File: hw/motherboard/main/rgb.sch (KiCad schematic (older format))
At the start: 68 parts, among them Q1 BSS138

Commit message: WIP Start motherboard PCB layout.
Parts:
- renumbered D6 to D10, D10 to D11, D14 to D12, D18 to D13, D22 to D14, D26 to D15, D30 to D16, D3 to D17, D7 to D18, D11 to D19, D5 to D2, D15 to D20, D19 to D21, D23 to D22, D27 to D23, D31 to D24, D4 to D25, D8 to D26, D12 to D27, D16 to D28, D20 to D29, D9 to D3, D24 to D30, D28 to D31, D13 to D4, D17 to D5, D21 to D6, D25 to D7, D29 to D8, D2 to D9
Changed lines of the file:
@@
 $EndComp
 $Comp
-L LED:WS2812B D5
+L LED:WS2812B D2
 U 1 1 5E462888
 P 5400 1700
-F 0 "D5" H 5450 2000 50  0000 L CNN
+F 0 "D2" H 5450 2000 50  0000 L CNN
 F 1 "WS2812B" H 5450 1400 50  0000 L CNN
 F 2 "LED_SMD:LED_WS2812B_PLCC4_5.0x5.0mm_P3.2mm" H 5450 1400 50  0001 L TNN
@@
 $EndComp
 $Comp
-L LED:WS2812B D9
+L LED:WS2812B D3
 U 1 1 5E462931
 P 6000 1700
-F 0 "D9" H 6050 2000 50  0000 L CNN
+F 0 "D3" H 6050 2000 50  0000 L CNN
 F 1 "WS2812B" H 6050 1400 50  0000 L CNN
 F 2 "LED_SMD:LED_WS2812B_PLCC4_5.0x5.0mm_P3.2mm" H 6050 1400 50  0001 L TNN
@@
 $EndComp
 $Comp
-L LED:WS2812B D13
+L LED:WS2812B D4
 U 1 1 5E462AA8
 P 6600 1700
-F 0 "D13" H 6650 2000 50  0000 L CNN
+F 0 "D4" H 6650 2000 50  0000 L CNN
 F 1 "WS2812B" H 6650 1400 50  0000 L CNN
 F 2 "LED_SMD:LED_WS2812B_PLCC4_5.0x5.0mm_P3.2mm" H 6650 1400 50  0001 L TNN
@@
 $EndComp
 $Comp
-L LED:WS2812B D17
+L LED:WS2812B D5
 U 1 1 5E462B55
 P 7200 1700
-F 0 "D17" H 7250 2000 50  0000 L CNN
+F 0 "D5" H 7250 2000 50  0000 L CNN
 F 1 "WS2812B" H 7250 1400 50  0000 L CNN
 F 2 "LED_SMD:LED_WS2812B_PLCC4_5.0x5.0mm_P3.2mm" H 7250 1400 50  0001 L TNN
@@
 $EndComp
 $Comp
-L LED:WS2812B D21
-U 1 1 5E462CD2
-P 7800 1700
-F 0 "D21" H 7850 2000 50  0000 L CNN
-F 1 "WS2812B" H 7850 1400 50  0000 L CNN
-F 2 "LED_SMD:LED_WS2812B_PLCC4_5.0x5.0mm_P3.2mm" H 7850 1400 50  0001 L TNN
-F 3 "https://cdn-shop.adafruit.com/datasheets/WS2812B.pdf" H 7900 1325 50  0001 L TNN
-	1    7800 1700
-	1    0    0    -1
-$EndComp
-$Comp
 L power:+5V #PWR065
 U 1 1 5E462CD9
@@
 $EndComp
 $Comp
-L LED:WS2812B D25
+L LED:WS2812B D7
 U 1 1 5E462D8B
 P 8400 1700
-F 0 "D25" H 8450 2000 50  0000 L CNN
+F 0 "D7" H 8450 2000 50  0000 L CNN
 F 1 "WS2812B" H 8450 1400 50  0000 L CNN
 F 2 "LED_SMD:LED_WS2812B_PLCC4_5.0x5.0mm_P3.2mm" H 8450 1400 50  0001 L TNN
@@
 $EndComp
 $Comp
-L LED:WS2812B D29
+L LED:WS2812B D8
 U 1 1 5E462E3E
 P 9000 1700
-F 0 "D29" H 9050 2000 50  0000 L CNN
+F 0 "D8" H 9050 2000 50  0000 L CNN
 F 1 "WS2812B" H 9050 1400 50  0000 L CNN
 F 2 "LED_SMD:LED_WS2812B_PLCC4_5.0x5.0mm_P3.2mm" H 9050 1400 50  0001 L TNN
@@
 $EndComp
 $Comp
-L LED:WS2812B D2
+L LED:WS2812B D9
 U 1 1 5E463575
 P 4800 2800
-F 0 "D2" H 4850 3100 50  0000 L CNN
+F 0 "D9" H 4850 3100 50  0000 L CNN
 F 1 "WS2812B" H 4850 2500 50  0000 L CNN
 F 2 "LED_SMD:LED_WS2812B_PLCC4_5.0x5.0mm_P3.2mm" H 4850 2500 50  0001 L TNN
@@
 $EndComp
 $Comp
-L LED:WS2812B D6
+L LED:WS2812B D10
 U 1 1 5E463588
 P 5400 2800
-F 0 "D6" H 5450 3100 50  0000 L CNN
+F 0 "D10" H 5450 3100 50  0000 L CNN
 F 1 "WS2812B" H 5450 2500 50  0000 L CNN
 F 2 "LED_SMD:LED_WS2812B_PLCC4_5.0x5.0mm_P3.2mm" H 5450 2500 50  0001 L TNN
@@
 $EndComp
 $Comp
-L LED:WS2812B D10
+L LED:WS2812B D11
 U 1 1 5E46359B
 P 6000 2800
-F 0 "D10" H 6050 3100 50  0000 L CNN
+F 0 "D11" H 6050 3100 50  0000 L CNN
 F 1 "WS2812B" H 6050 2500 50  0000 L CNN
 F 2 "LED_SMD:LED_WS2812B_PLCC4_5.0x5.0mm_P3.2mm" H 6050 2500 50  0001 L TNN
@@
 $EndComp
 $Comp
-L LED:WS2812B D14
+L LED:WS2812B D12
 U 1 1 5E4635AE
 P 6600 2800
-F 0 "D14" H 6650 3100 50  0000 L CNN
+F 0 "D12" H 6650 3100 50  0000 L CNN
 F 1 "WS2812B" H 6650 2500 50  0000 L CNN
 F 2 "LED_SMD:LED_WS2812B_PLCC4_5.0x5.0mm_P3.2mm" H 6650 2500 50  0001 L TNN
@@
 $EndComp
 $Comp
-L LED:WS2812B D18
+L LED:WS2812B D13
 U 1 1 5E4635C1
 P 7200 2800
-F 0 "D18" H 7250 3100 50  0000 L CNN
+F 0 "D13" H 7250 3100 50  0000 L CNN
 F 1 "WS2812B" H 7250 2500 50  0000 L CNN
 F 2 "LED_SMD:LED_WS2812B_PLCC4_5.0x5.0mm_P3.2mm" H 7250 2500 50  0001 L TNN
@@
 $EndComp
 $Comp
-L LED:WS2812B D22
+L LED:WS2812B D14
 U 1 1 5E4635D4
 P 7800 2800
-F 0 "D22" H 7850 3100 50  0000 L CNN
+F 0 "D14" H 7850 3100 50  0000 L CNN
 F 1 "WS2812B" H 7850 2500 50  0000 L CNN
 F 2 "LED_SMD:LED_WS2812B_PLCC4_5.0x5.0mm_P3.2mm" H 7850 2500 50  0001 L TNN
@@
 $EndComp
 $Comp
-L LED:WS2812B D26
+L LED:WS2812B D15
 U 1 1 5E4635E7
 P 8400 2800
-F 0 "D26" H 8450 3100 50  0000 L CNN
+F 0 "D15" H 8450 3100 50  0000 L CNN
 F 1 "WS2812B" H 8450 2500 50  0000 L CNN
 F 2 "LED_SMD:LED_WS2812B_PLCC4_5.0x5.0mm_P3.2mm" H 8450 2500 50  0001 L TNN
@@
 $EndComp
 $Comp
-L LED:WS2812B D30
+L LED:WS2812B D16
 U 1 1 5E4635FA
 P 9000 2800
-F 0 "D30" H 9050 3100 50  0000 L CNN
+F 0 "D16" H 9050 3100 50  0000 L CNN
 F 1 "WS2812B" H 9050 2500 50  0000 L CNN
 F 2 "LED_SMD:LED_WS2812B_PLCC4_5.0x5.0mm_P3.2mm" H 9050 2500 50  0001 L TNN
@@
 Logic level conversion (3.3V to 5V)
 $Comp
-L LED:WS2812B D3
+L LED:WS2812B D17
 U 1 1 5E466593
 P 4800 3900
-F 0 "D3" H 4850 4200 50  0000 L CNN
+F 0 "D17" H 4850 4200 50  0000 L CNN
 F 1 "WS2812B" H 4850 3600 50  0000 L CNN
 F 2 "LED_SMD:LED_WS2812B_PLCC4_5.0x5.0mm_P3.2mm" H 4850 3600 50  0001 L TNN
@@
 $EndComp
 $Comp
-L LED:WS2812B D7
+L LED:WS2812B D18
 U 1 1 5E4665A7
 P 5400 3900
-F 0 "D7" H 5450 4200 50  0000 L CNN
+F 0 "D18" H 5450 4200 50  0000 L CNN
 F 1 "WS2812B" H 5450 3600 50  0000 L CNN
 F 2 "LED_SMD:LED_WS2812B_PLCC4_5.0x5.0mm_P3.2mm" H 5450 3600 50  0001 L TNN
@@
 $EndComp
 $Comp
-L LED:WS2812B D11
+L LED:WS2812B D19
 U 1 1 5E4665BA
 P 6000 3900
-F 0 "D11" H 6050 4200 50  0000 L CNN
+F 0 "D19" H 6050 4200 50  0000 L CNN
 F 1 "WS2812B" H 6050 3600 50  0000 L CNN
 F 2 "LED_SMD:LED_WS2812B_PLCC4_5.0x5.0mm_P3.2mm" H 6050 3600 50  0001 L TNN
@@
 $EndComp
 $Comp
-L LED:WS2812B D15
+L LED:WS2812B D20
 U 1 1 5E4665CD
 P 6600 3900
-F 0 "D15" H 6650 4200 50  0000 L CNN
+F 0 "D20" H 6650 4200 50  0000 L CNN
 F 1 "WS2812B" H 6650 3600 50  0000 L CNN
 F 2 "LED_SMD:LED_WS2812B_PLCC4_5.0x5.0mm_P3.2mm" H 6650 3600 50  0001 L TNN
@@
 $EndComp
 $Comp
-L LED:WS2812B D19
+L LED:WS2812B D21
 U 1 1 5E4665E0
 P 7200 3900
-F 0 "D19" H 7250 4200 50  0000 L CNN
+F 0 "D21" H 7250 4200 50  0000 L CNN
 F 1 "WS2812B" H 7250 3600 50  0000 L CNN
 F 2 "LED_SMD:LED_WS2812B_PLCC4_5.0x5.0mm_P3.2mm" H 7250 3600 50  0001 L TNN
@@
 $EndComp
 $Comp
-L LED:WS2812B D23
+L LED:WS2812B D22
 U 1 1 5E4665F3
 P 7800 3900
-F 0 "D23" H 7850 4200 50  0000 L CNN
+F 0 "D22" H 7850 4200 50  0000 L CNN
 F 1 "WS2812B" H 7850 3600 50  0000 L CNN
 F 2 "LED_SMD:LED_WS2812B_PLCC4_5.0x5.0mm_P3.2mm" H 7850 3600 50  0001 L TNN
@@
 $EndComp
 $Comp
-L LED:WS2812B D27
+L LED:WS2812B D23
 U 1 1 5E466606
 P 8400 3900
-F 0 "D27" H 8450 4200 50  0000 L CNN
+F 0 "D23" H 8450 4200 50  0000 L CNN
 F 1 "WS2812B" H 8450 3600 50  0000 L CNN
 F 2 "LED_SMD:LED_WS2812B_PLCC4_5.0x5.0mm_P3.2mm" H 8450 3600 50  0001 L TNN
@@
 $EndComp
 $Comp
-L LED:WS2812B D31
+L LED:WS2812B D24
 U 1 1 5E466619
 P 9000 3900
-F 0 "D31" H 9050 4200 50  0000 L CNN
+F 0 "D24" H 9050 4200 50  0000 L CNN
 F 1 "WS2812B" H 9050 3600 50  0000 L CNN
 F 2 "LED_SMD:LED_WS2812B_PLCC4_5.0x5.0mm_P3.2mm" H 9050 3600 50  0001 L TNN
@@
 $EndComp
 $Comp
-L LED:WS2812B D4
+L LED:WS2812B D25
 U 1 1 5E46662C
 P 4800 5000
-F 0 "D4" H 4850 5300 50  0000 L CNN
+F 0 "D25" H 4850 5300 50  0000 L CNN
 F 1 "WS2812B" H 4850 4700 50  0000 L CNN
 F 2 "LED_SMD:LED_WS2812B_PLCC4_5.0x5.0mm_P3.2mm" H 4850 4700 50  0001 L TNN
@@
 $EndComp
 $Comp
-L LED:WS2812B D8
+L LED:WS2812B D26
 U 1 1 5E46663F
 P 5400 5000
-F 0 "D8" H 5450 5300 50  0000 L CNN
+F 0 "D26" H 5450 5300 50  0000 L CNN
 F 1 "WS2812B" H 5450 4700 50  0000 L CNN
 F 2 "LED_SMD:LED_WS2812B_PLCC4_5.0x5.0mm_P3.2mm" H 5450 4700 50  0001 L TNN
@@
 $EndComp
 $Comp
-L LED:WS2812B D12
+L LED:WS2812B D27
 U 1 1 5E466652
 P 6000 5000
-F 0 "D12" H 6050 5300 50  0000 L CNN
+F 0 "D27" H 6050 5300 50  0000 L CNN
 F 1 "WS2812B" H 6050 4700 50  0000 L CNN
 F 2 "LED_SMD:LED_WS2812B_PLCC4_5.0x5.0mm_P3.2mm" H 6050 4700 50  0001 L TNN
@@
 $EndComp
 $Comp
-L LED:WS2812B D16
+L LED:WS2812B D28
 U 1 1 5E466665
 P 6600 5000
-F 0 "D16" H 6650 5300 50  0000 L CNN
+F 0 "D28" H 6650 5300 50  0000 L CNN
 F 1 "WS2812B" H 6650 4700 50  0000 L CNN
 F 2 "LED_SMD:LED_WS2812B_PLCC4_5.0x5.0mm_P3.2mm" H 6650 4700 50  0001 L TNN
@@
 $EndComp
 $Comp
-L LED:WS2812B D20
+L LED:WS2812B D29
 U 1 1 5E466678
 P 7200 5000
-F 0 "D20" H 7250 5300 50  0000 L CNN
+F 0 "D29" H 7250 5300 50  0000 L CNN
 F 1 "WS2812B" H 7250 4700 50  0000 L CNN
 F 2 "LED_SMD:LED_WS2812B_PLCC4_5.0x5.0mm_P3.2mm" H 7250 4700 50  0001 L TNN
@@
 $EndComp
 $Comp
-L LED:WS2812B D24
+L LED:WS2812B D30
 U 1 1 5E46668B
 P 7800 5000
-F 0 "D24" H 7850 5300 50  0000 L CNN
+F 0 "D30" H 7850 5300 50  0000 L CNN
 F 1 "WS2812B" H 7850 4700 50  0000 L CNN
 F 2 "LED_SMD:LED_WS2812B_PLCC4_5.0x5.0mm_P3.2mm" H 7850 4700 50  0001 L TNN
@@
 $EndComp
 $Comp
-L LED:WS2812B D28
+L LED:WS2812B D31
 U 1 1 5E46669E
 P 8400 5000
-F 0 "D28" H 8450 5300 50  0000 L CNN
+F 0 "D31" H 8450 5300 50  0000 L CNN
 F 1 "WS2812B" H 8450 4700 50  0000 L CNN
 F 2 "LED_SMD:LED_WS2812B_PLCC4_5.0x5.0mm_P3.2mm" H 8450 4700 50  0001 L TNN
@@
 Wire Wire Line
 	3400 1700 4000 1700
+$Comp
+L LED:WS2812B D6
+U 1 1 5E462CD2
+P 7800 1700
+F 0 "D6" H 7850 2000 50  0000 L CNN
+F 1 "WS2812B" H 7850 1400 50  0000 L CNN
+F 2 "LED_SMD:LED_WS2812B_PLCC4_5.0x5.0mm_P3.2mm" H 7850 1400 50  0001 L TNN
+F 3 "https://cdn-shop.adafruit.com/datasheets/WS2812B.pdf" H 7900 1325 50  0001 L TNN
+	1    7800 1700
+	1    0    0    -1
+$EndComp
 $EndSCHEMATC

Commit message: WIP Add electromagnet and sensor schematic connections to MCU pins
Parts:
- added C46: 1000u, Capacitor_THT:CP_Radial_D10.0mm_P5.00mm, symbol Device:CP
- added J5: RGB stack, Connector_PinSocket_2.54mm:PinSocket_1x02_P2.54mm_Vertical, symbol Connector:Conn_01x02_Female
- added SW2: SW_SPDT, Connector_PinHeader_2.54mm:PinHeader_1x03_P2.54mm_Vertical, symbol Switch:SW_SPDT
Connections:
- net +5V: now also SW2.3 (C); no longer C14.1, C15.1, C16.1, C17.1, C18.1, C19.1, C20.1, C21.1, C22.1, C23.1, C24.1, C25.1, C26.1, C27.1, C28.1, C29.1, C30.1, C31.1, C32.1, C33.1, C34.1, C35.1, C36.1, C37.1, C38.1, C39.1, C40.1, C41.1, C42.1, C43.1, C44.1, C45.1, D1.1 (VDD), D10.1 (VDD), D11.1 (VDD), D12.1 (VDD), D13.1 (VDD), D14.1 (VDD), D15.1 (VDD), D16.1 (VDD), D17.1 (VDD), D18.1 (VDD), D19.1 (VDD), D2.1 (VDD), D20.1 (VDD), D21.1 (VDD), D22.1 (VDD), D23.1 (VDD), D24.1 (VDD), D25.1 (VDD), D26.1 (VDD), D27.1 (VDD), D28.1 (VDD), D29.1 (VDD), D3.1 (VDD), D30.1 (VDD), D31.1 (VDD), D32.1 (VDD), D4.1 (VDD), D5.1 (VDD), D6.1 (VDD), D7.1 (VDD), D8.1 (VDD), D9.1 (VDD), R4.1
- net GND: now also C46.2
- net at D32.2 (DOUT): now also J5.2 (Pin_2)
- new net 5V_RGB: C14.1, C15.1, C16.1, C17.1, C18.1, C19.1, C20.1, C21.1, C22.1, C23.1, C24.1, C25.1, C26.1, C27.1, C28.1, C29.1, C30.1, C31.1, C32.1, C33.1, C34.1, C35.1, C36.1, C37.1, C38.1, C39.1, C40.1, C41.1, C42.1, C43.1, C44.1, C45.1, C46.1, D1.1 (VDD), D10.1 (VDD), D11.1 (VDD), D12.1 (VDD), D13.1 (VDD), D14.1 (VDD), D15.1 (VDD), D16.1 (VDD), D17.1 (VDD), D18.1 (VDD), D19.1 (VDD), D2.1 (VDD), D20.1 (VDD), D21.1 (VDD), D22.1 (VDD), D23.1 (VDD), D24.1 (VDD), D25.1 (VDD), D26.1 (VDD), D27.1 (VDD), D28.1 (VDD), D29.1 (VDD), D3.1 (VDD), D30.1 (VDD), D31.1 (VDD), D32.1 (VDD), D4.1 (VDD), D5.1 (VDD), D6.1 (VDD), D7.1 (VDD), D8.1 (VDD), D9.1 (VDD), J5.1 (Pin_1), R4.1, SW2.2 (B)
- no-connect marks 0 -> 1
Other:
- note added: "LED power switch and \ninput capacitor"
- note removed: "TODO: data output to relelauta\nthrough stack connector"

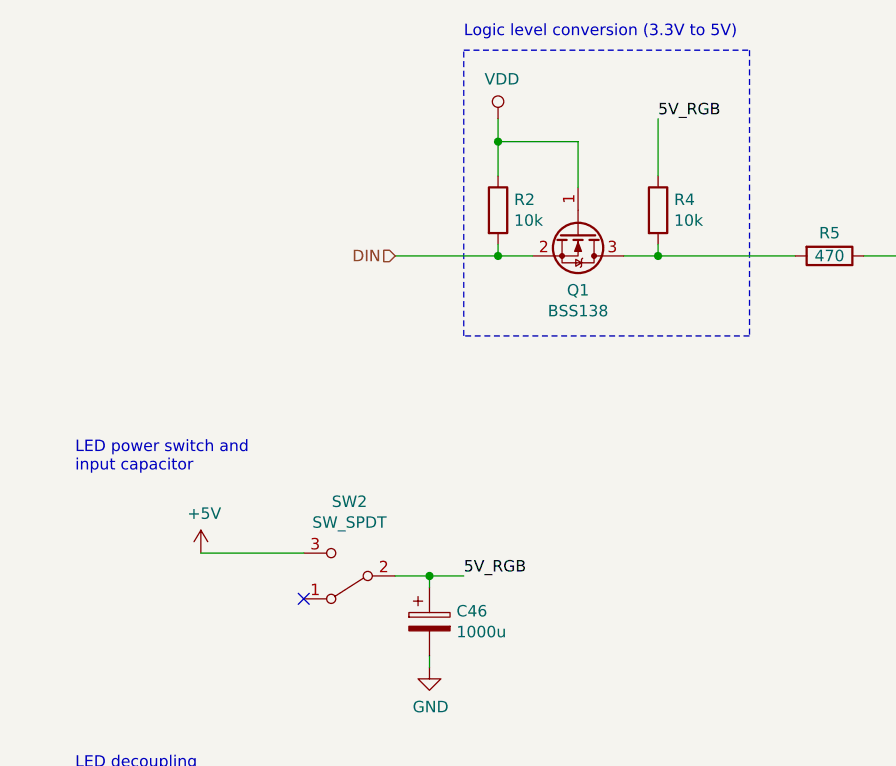
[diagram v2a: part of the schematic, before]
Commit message: Minor motherboard layout changes. Bump revision number to 1.1.
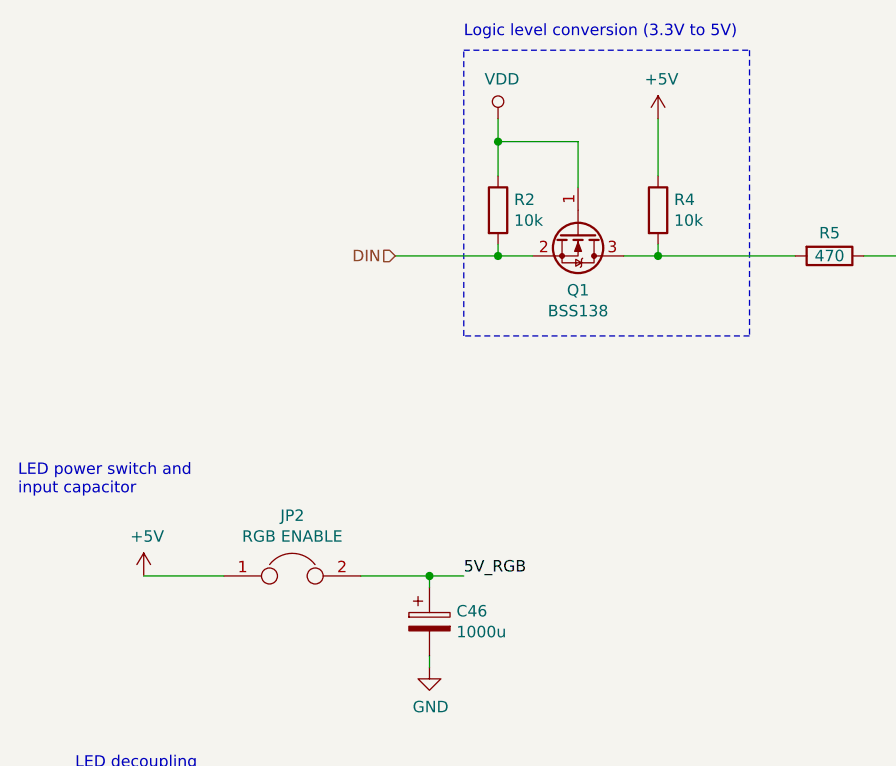
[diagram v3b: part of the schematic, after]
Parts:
- removed SW2: SW_SPDT, Connector_PinHeader_2.54mm:PinHeader_1x03_P2.54mm_Vertical, symbol Switch:SW_SPDT
- added JP2: RGB ENABLE, Connector_PinHeader_2.54mm:PinHeader_1x02_P2.54mm_Vertical, symbol Device:Jumper
- C46: footprint Capacitor_THT:CP_Radial_D10.0mm_P5.00mm -> Capacitor_SMD:CP_Elec_10x10
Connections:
- net +5V: now also R4.1, JP2.1
- net 5V_RGB: now also JP2.2; no longer R4.1
- no-connect marks 1 -> 0
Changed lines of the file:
@@
 encoding utf-8
 Sheet 2 4
-Title "KAPINE Motherboard RGB"
-Date ""
-Rev "1"
+Title "KAPINE Motherboard"
+Date "2020-09-02"
+Rev "1.1"
 Comp "Verneri Hirvonen"
 Comment1 ""
@@
 Text Label 1050 6500 0    50   ~ 0
 5V_RGB
-$Comp
-L Switch:SW_SPDT SW2
-U 1 1 5F581FDB
-P 2050 3100
-F 0 "SW2" H 2050 2775 50  0000 C CNN
-F 1 "SW_SPDT" H 2050 2866 50  0000 C CNN
-F 2 "Connector_PinHeader_2.54mm:PinHeader_1x03_P2.54mm_Vertical" H 2050 3100 50  0001 C CNN
-F 3 "~" H 2050 3100 50  0001 C CNN
-	1    2050 3100
-	-1   0    0    1
-$EndComp
 Wire Wire Line
 	2400 3150 2400 3100
@@
 $EndComp
 Wire Wire Line
-	1400 3000 1850 3000
-NoConn ~ 1850 3200
+	1150 3100 1500 3100
 Text Label 2550 3100 0    50   ~ 0
 5V_RGB
@@
 Connection ~ 2400 3100
 Wire Wire Line
-	2400 3100 2250 3100
+	2400 3100 2100 3100
 $Comp
 L power:+5V #PWR025
 U 1 1 5F5D5CD4
-P 1400 3000
-F 0 "#PWR025" H 1400 2850 50  0001 C CNN
-F 1 "+5V" H 1415 3173 50  0000 C CNN
-F 2 "" H 1400 3000 50  0001 C CNN
-F 3 "" H 1400 3000 50  0001 C CNN
-	1    1400 3000
-	1    0    0    -1
-$EndComp
-Text Notes 850  2650 0    50   ~ 0
+P 1150 3100
+F 0 "#PWR025" H 1150 2950 50  0001 C CNN
+F 1 "+5V" H 1165 3273 50  0000 C CNN
+F 2 "" H 1150 3100 50  0001 C CNN
+F 3 "" H 1150 3100 50  0001 C CNN
+	1    1150 3100
+	1    0    0    -1
+$EndComp
+Text Notes 600  2750 0    50   ~ 0
 LED power switch and \ninput capacitor
 $Comp
@@
 F 0 "C46" H 2518 3346 50  0000 L CNN
 F 1 "1000u" H 2518 3255 50  0000 L CNN
-F 2 "Capacitor_THT:CP_Radial_D10.0mm_P5.00mm" H 2438 3150 50  0001 C CNN
+F 2 "Capacitor_SMD:CP_Elec_10x10" H 2438 3150 50  0001 C CNN
 F 3 "~" H 2400 3300 50  0001 C CNN
 	1    2400 3300
 	1    0    0    -1
 $EndComp
-Text Label 3400 1100 0    50   ~ 0
-5V_RGB
 Wire Notes Line
 	3800 2050 2550 2050
+$Comp
+L Device:Jumper JP2
+U 1 1 5F69E68B
+P 1800 3100
+F 0 "JP2" H 1800 3364 50  0000 C CNN
+F 1 "RGB ENABLE" H 1800 3273 50  0000 C CNN
+F 2 "Connector_PinHeader_2.54mm:PinHeader_1x02_P2.54mm_Vertical" H 1800 3100 50  0001 C CNN
+F 3 "~" H 1800 3100 50  0001 C CNN
+	1    1800 3100
+	1    0    0    -1
+$EndComp
+$Comp
+L power:+5V #PWR016
+U 1 1 5F6DB28F
+P 3400 1100
+F 0 "#PWR016" H 3400 950 50  0001 C CNN
+F 1 "+5V" H 3415 1273 50  0000 C CNN
+F 2 "" H 3400 1100 50  0001 C CNN
+F 3 "" H 3400 1100 50  0001 C CNN
+	1    3400 1100
+	1    0    0    -1
+$EndComp
 $EndSCHEMATC
